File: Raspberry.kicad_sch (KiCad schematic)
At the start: 31 parts, among them J11 CAN, J18 SPARE_RASPI, J19 Raspberry_Pi_2_3, J20 RASPI_FAN, Q16 2N7002NXAK, Q2 2N7002NXAK, U3 PCA9634PW,118, U4 MCP2515-xSO, U5 MCP2562-E-SN, Y1 16MHz

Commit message: First version of the pcb layout
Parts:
- J11: footprint Connector_Molex:Molex_Micro-Fit_3.0_43650-0300_1x03_P3.00mm_Horizontal -> Connector_Molex:Molex_Micro-Fit_3.0_43650-0315_1x03_P3.00mm_Vertical
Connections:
- net at R8.2, U5.6 (CANL): now also J11.1 (Pin_1); no longer J11.2 (Pin_2)
- net at R8.1, U5.7 (CANH): now also J11.2 (Pin_2); no longer J11.1 (Pin_1)
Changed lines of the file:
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@@
     (stroke (width 0) (type default) (color 0 0 0 0))
   )
-  (wire (pts (xy 265.43 46.99) (xy 265.43 41.91))
+  (wire (pts (xy 265.43 41.91) (xy 265.43 49.53))
     (stroke (width 0) (type default) (color 0 0 0 0))
   )
@@
     (stroke (width 0) (type default) (color 0 0 0 0))
   )
+  (wire (pts (xy 266.7 46.99) (xy 270.51 46.99))
+    (stroke (width 0) (type default) (color 0 0 0 0))
+  )
   (wire (pts (xy 237.49 25.4) (xy 237.49 27.94))
     (stroke (width 0) (type default) (color 0 0 0 0))
@@
     (stroke (width 0) (type default) (color 0 0 0 0))
   )
+  (wire (pts (xy 265.43 49.53) (xy 270.51 49.53))
+    (stroke (width 0) (type default) (color 0 0 0 0))
+  )
   (wire (pts (xy 219.71 40.64) (xy 219.71 45.72))
     (stroke (width 0) (type default) (color 0 0 0 0))
@@
     (stroke (width 0) (type default) (color 0 0 0 0))
   )
-  (wire (pts (xy 256.54 54.61) (xy 265.43 54.61))
+  (wire (pts (xy 256.54 54.61) (xy 266.7 54.61))
     (stroke (width 0) (type default) (color 0 0 0 0))
   )
@@
     (stroke (width 0) (type default) (color 0 0 0 0))
   )
-  (wire (pts (xy 265.43 54.61) (xy 265.43 49.53))
-    (stroke (width 0) (type default) (color 0 0 0 0))
-  )
   (wire (pts (xy 78.74 173.99) (xy 81.28 173.99))
     (stroke (width 0) (type default) (color 0 0 0 0))
@@
     (stroke (width 0) (type default) (color 0 0 0 0))
   )
+  (wire (pts (xy 266.7 54.61) (xy 266.7 46.99))
+    (stroke (width 0) (type default) (color 0 0 0 0))
+  )
   (wire (pts (xy 62.23 27.94) (xy 62.23 29.21))
     (stroke (width 0) (type default) (color 0 0 0 0))
@@
     (stroke (width 0) (type default) (color 0 0 0 0))
   )
-  (wire (pts (xy 265.43 49.53) (xy 270.51 49.53))
-    (stroke (width 0) (type default) (color 0 0 0 0))
-  )
-  (wire (pts (xy 270.51 46.99) (xy 265.43 46.99))
-    (stroke (width 0) (type default) (color 0 0 0 0))
-  )
   (wire (pts (xy 64.77 114.3) (xy 66.04 114.3))
     (stroke (width 0) (type default) (color 0 0 0 0))
@@
     (stroke (width 0) (type default) (color 0 0 0 0))
   )
+  (wire (pts (xy 86.36 100.33) (xy 102.87 100.33))
+    (stroke (width 0) (type default) (color 0 0 0 0))
+  )
   (wire (pts (xy 39.37 173.99) (xy 50.8 173.99))
     (stroke (width 0) (type default) (color 0 0 0 0))
   )
   (wire (pts (xy 45.72 179.07) (xy 50.8 179.07))
-    (stroke (width 0) (type default) (color 0 0 0 0))
-  )
-  (wire (pts (xy 86.36 100.33) (xy 102.87 100.33))
     (stroke (width 0) (type default) (color 0 0 0 0))
   )
@@
     (effects (font (size 1.27 1.27)) (justify right bottom))
   )
-  (label "NC_RASP_5" (at 102.87 100.33 180)
-    (effects (font (size 1.27 1.27)) (justify right bottom))
-  )
   (label "RASPY_FAN_PWM" (at 120.015 184.15 180)
     (effects (font (size 1.27 1.27)) (justify right bottom))
@@
   (label "RASP_CLK" (at 152.4 48.26 0)
     (effects (font (size 1.27 1.27)) (justify left bottom))
+  )
+  (label "NC_RASP_5" (at 102.87 100.33 180)
+    (effects (font (size 1.27 1.27)) (justify right bottom))
   )
   (hierarchical_label "BUT_4" (shape input) (at 38.1 97.79 180)
@@
       (effects (font (size 1.27 1.27)) (justify left))
     )
-    (property "Footprint" "Connector_Molex:Molex_Micro-Fit_3.0_43650-0300_1x03_P3.00mm_Horizontal" (id 2) (at 275.59 49.53 0)
-      (effects (font (size 1.27 1.27)) hide)
-    )
+    (property "Footprint" "Connector_Molex:Molex_Micro-Fit_3.0_43650-0315_1x03_P3.00mm_Vertical" (id 2) (at 275.59 49.53 0)
+      (effects (font (size 1.27 1.27)) hide)
+    )

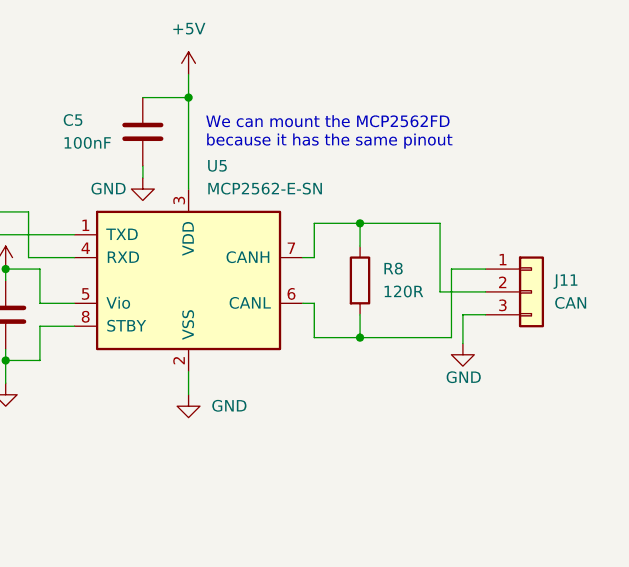
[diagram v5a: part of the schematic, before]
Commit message: Second iteration of the board layout. Need to fix some traces
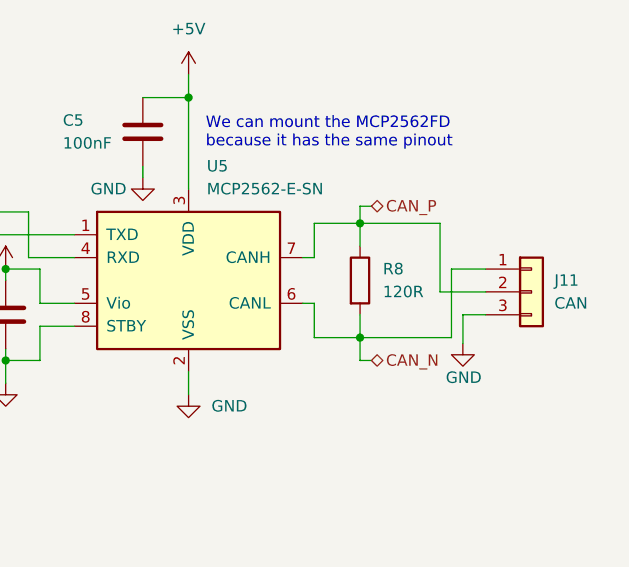
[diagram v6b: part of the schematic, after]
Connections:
- net CAN_N: now reaches J11.1 (Pin_1), R8.2, U5.6 (CANL)
- net CAN_P: now reaches J11.2 (Pin_2), R8.1, U5.7 (CANH)

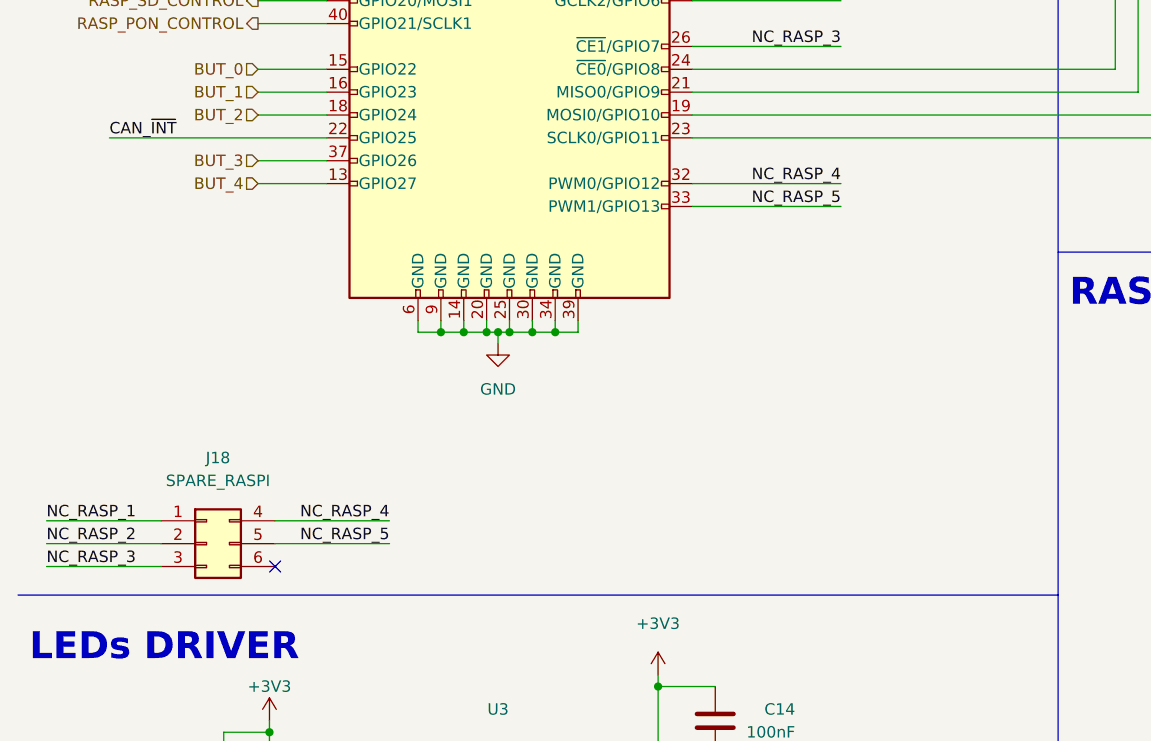
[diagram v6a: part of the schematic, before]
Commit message: Added connector, fixed traces, first version of silkscreen
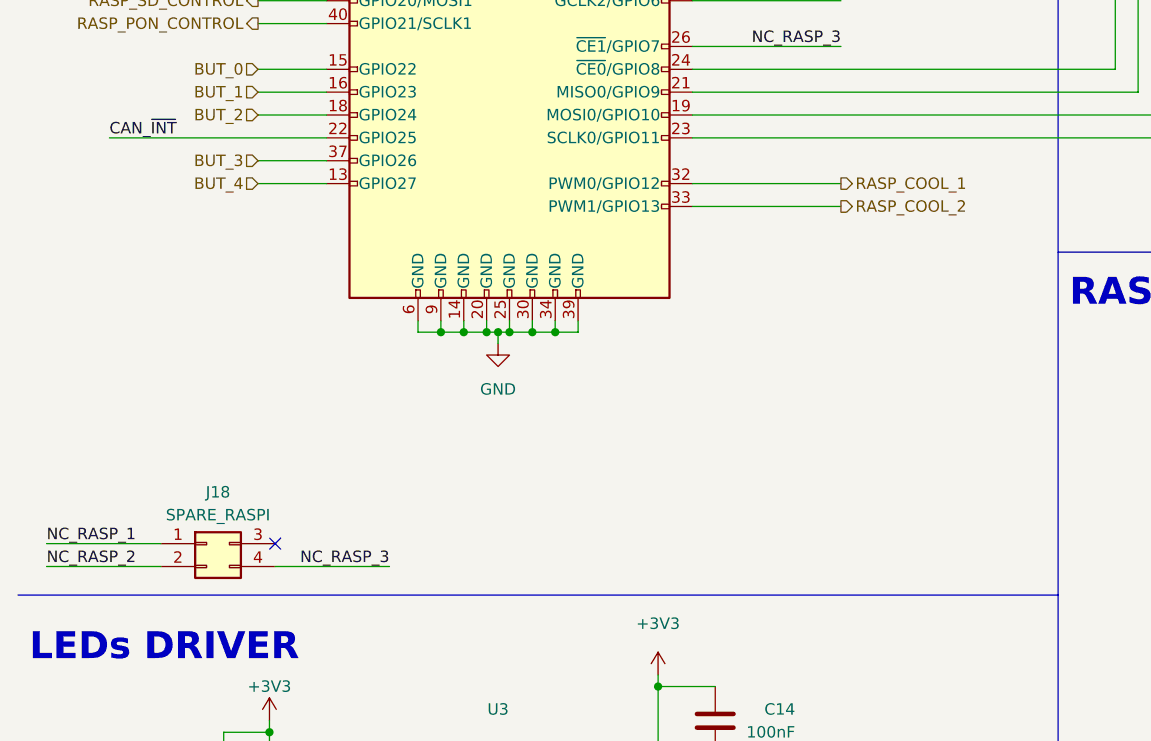
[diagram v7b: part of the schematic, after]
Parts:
- J18: footprint Connector_Molex:Molex_Micro-Fit_3.0_43045-0612_2x03_P3.00mm_Vertical -> Connector_Molex:Molex_Micro-Fit_3.0_43045-0412_2x02_P3.00mm_Vertical; symbol Connector_Generic:Conn_02x03_Top_Bottom -> Connector_Generic:Conn_02x02_Top_Bottom
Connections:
- net NC_RASP_3: now also J18.4 (Pin_4); no longer J18.3 (Pin_3)
- net NC_RASP_4 renamed RASP_COOL_1
- net RASP_COOL_1: no longer J18.4 (Pin_4)
- net NC_RASP_5 renamed RASP_COOL_2
- net RASP_COOL_2: no longer J18.5 (Pin_5)

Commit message: Fixed Schematic, fixed some traces. Still not finished
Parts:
- removed C11, C14: 100nF, Resistor_SMD:R_0805_2012Metric, symbol Device:C
- removed U3: PCA9634PW,118, 00_proj-lib:SOP65P640X110-20N, symbol 00_proj-lib:PCA9634PW,118
- added R37: 22R, Resistor_SMD:R_0603_1608Metric, symbol Device:R
- C1, C2: footprint Resistor_SMD:R_0603_1608Metric -> Capacitor_SMD:C_0603_1608Metric
- C12, C13, C3, C4, C5: footprint Resistor_SMD:R_0805_2012Metric -> Capacitor_SMD:C_0603_1608Metric
- D17, D2: footprint Diode_SMD:D_SOD-323_HandSoldering -> Diode_SMD:D_SOD-123
- Y1: footprint Crystal:Crystal_HC49-4H_Vertical -> Crystal:Crystal_SMD_3225-4Pin_3.2x2.5mm; symbol Device:Crystal -> Device:Crystal_GND24; Campo4 (none) -> ECS-160-18-33-AEN-TR
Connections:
- net GND: now also J18.3 (Pin_3), Y1.2, Y1.4
- new net: C2.1, R37.2, Y1.3
- new net: R37.1, U4.8 (OSC1)
- no-connect marks 8 -> 7
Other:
- note removed: "Address: 0010 101X"
- note removed: "LEDs DRIVER"
- moved on the sheet: BZ1, C1, C12, C13, C2, D17, D2, J18, J19, J20, JP2, Q16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
